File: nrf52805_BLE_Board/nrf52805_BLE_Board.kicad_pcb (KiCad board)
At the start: 2 copper layers, 27 parts, among them J1 TSW-103-23-H-S, J2 10118194-0001LF, J3 3220-10-0100-00, J4 TSW-107-23-H-S, J5 TSW-107-23-H-S, U1 BC805M, U2 CP2102N-Axx-xQFN28, U3 TCR3DF33_LMCT, Y1 CM9V-T1A-32.768KHZ-9PF-20PPM-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

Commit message: Finish layout
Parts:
- moved U2 193.4 mm to (58.0, 63.0), turned to 90 degrees
- moved J4 168.8 mm to (51.5, 45.5), turned to -90 degrees
- moved R5 150.0 mm to (57.9, 50.6)
- moved J5 149.6 mm to (71.4, 60.7), turned to 90 degrees
- moved L1 143.6 mm to (55.0, 74.4), turned to 90 degrees
- moved R3 143.2 mm to (70.5, 31.5)
- moved R4 142.6 mm to (70.5, 35.5)
- moved R2 142.3 mm to (59.8, 72.0)
- moved C7 140.3 mm to (64.5, 41.9), turned to 180 degrees
- moved L2 140.1 mm to (59.8, 70.0), turned to 180 degrees
- moved C8 138.7 mm to (70.5, 33.5), turned to 180 degrees
- moved R1 138.5 mm to (64.5, 60.1)
- moved C9 138.1 mm to (70.5, 37.5), turned to 180 degrees
- moved C6 136.0 mm to (59.8, 73.8)
- moved S1 134.8 mm to (52.3, 35.5), turned to 90 degrees
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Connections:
- C5 pad 1: unconnected-(C5-Pad1) -> Net-(C5-Pad1)
- R2 pad 2: unconnected-(R2-Pad2) -> Net-(R2-Pad2)
- U1 pad 2: /SWCLK -> /SWDCLK
- U3 pad 1: unconnected-(U3-Pad1) -> Net-(C6-Pad1)
- U3 pad 2: unconnected-(U3-Pad2) -> GND
- U3 pad 3: unconnected-(U3-Pad3) -> Net-(R2-Pad2)
- U3 pad 4: unconnected-(U3-Pad4) -> Net-(C5-Pad1)
- U3 pad 5: unconnected-(U3-Pad5) -> +3V3
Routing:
- net /P021: track 0.00 -> 51.5 mm
- net GND: track 0.00 -> 49.4 mm, vias 0 -> 53
- net +3V3: track 0.00 -> 49.1 mm, vias 0 -> 2
- net /P012: track 0.00 -> 43.9 mm
- net /P016: track 0.00 -> 39.1 mm, vias 0 -> 1
- net /SWDIO: track 0.00 -> 38.7 mm, vias 0 -> 5
- net /SWDCLK: track 0.00 -> 36.7 mm, vias 0 -> 3
- net /P020: track 0.00 -> 25.0 mm, vias 0 -> 2
- net /P005: track 0.00 -> 22.4 mm
- net /P018: track 0.00 -> 21.5 mm
- net /P014: track 0.00 -> 21.1 mm
- net /P004: track 0.00 -> 20.0 mm
- net /P000: track 0.00 -> 19.9 mm, vias 0 -> 1
- net /P001: track 0.00 -> 18.7 mm, vias 0 -> 1
- net Net-(U2-VBUS): track 0.00 -> 17.6 mm
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- added copper zone on B.Cu, net GND
- added copper zone on F.Cu, net GND
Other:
- board outline added: 22.9 x 50.8 mm

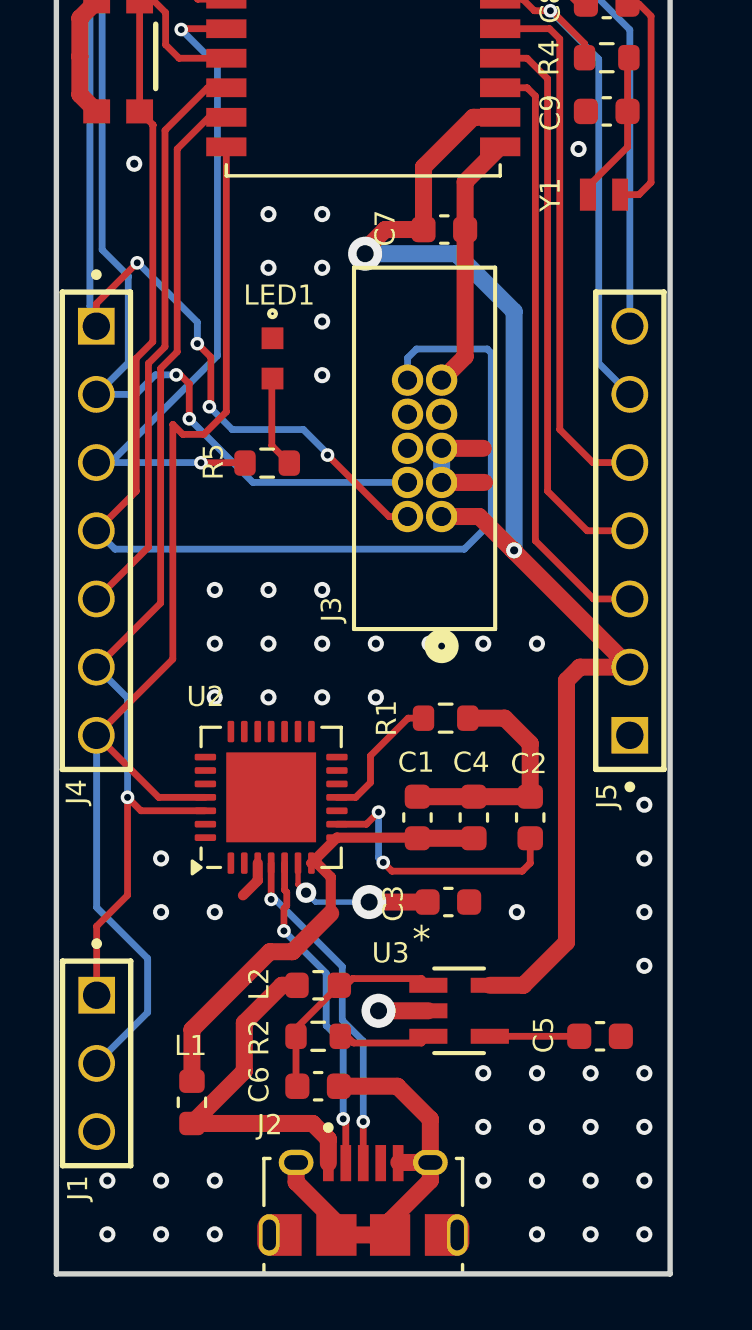
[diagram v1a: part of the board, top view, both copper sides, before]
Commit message: Add fiducials and silkscreen markings
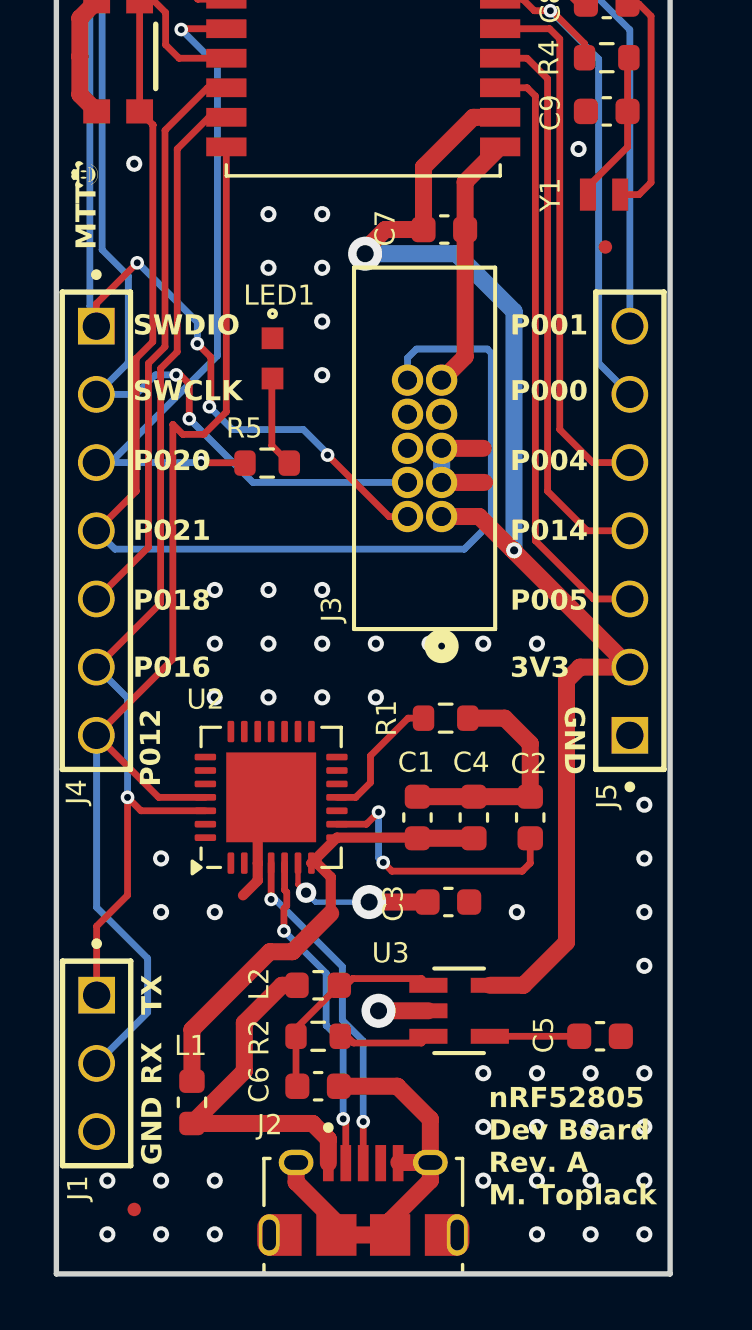
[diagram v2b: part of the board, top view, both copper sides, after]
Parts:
- added FD1: Fiducial, Fiducial:Fiducial_0.5mm_Mask1mm, F.Cu at (52.9, 78.4)
- added FD2: Fiducial, Fiducial:Fiducial_0.5mm_Mask1mm, F.Cu at (70.5, 42.5)
- added G***: LOGO, LOGO, F.Cu at (51.0, 39.9)
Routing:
- net GND: track 49.4 -> 52.0 mm
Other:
- board text added: "3V3"
- board text added: "GND"
- board text added: "MTT"
- board text added: "Matthew T. Toplack Design Fanstel BC805M Based nRF52805 Development Board"
- board text added: "P000"
- board text added: "P001"
- board text added: "P004"
- board text added: "P005"
- board text added: "P012"
- board text added: "P014"
- board text added: "P016"
- board text added: "P018"
- board text added: "P020"
- board text added: "P021"
- board text added: "RX"
- board text added: "SWCLK"
- board text added: "SWDIO"
- board text added: "TX"
- board text added: "nRF52805 Dev Board Rev. A M. Toplack"

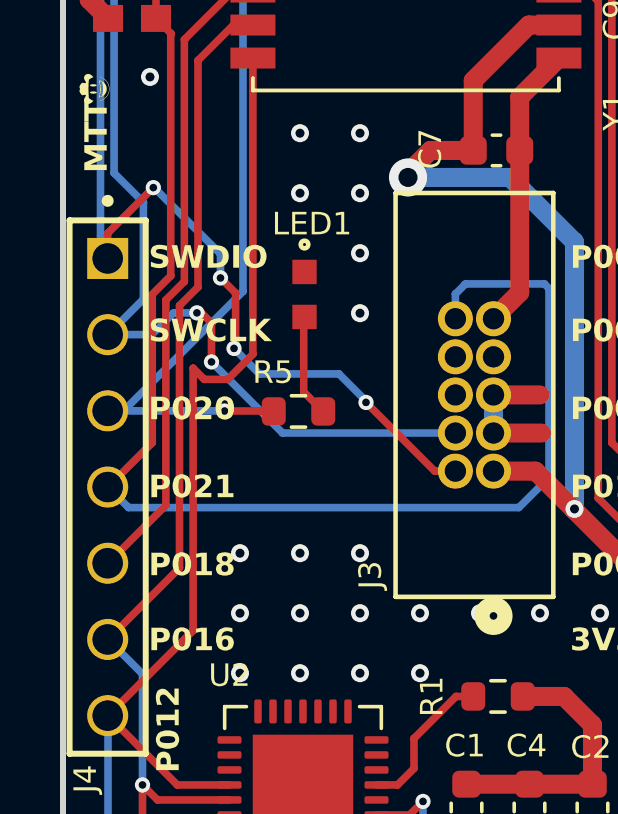
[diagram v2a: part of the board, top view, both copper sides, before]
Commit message: Correct issue with traces, add fiducials to schematic
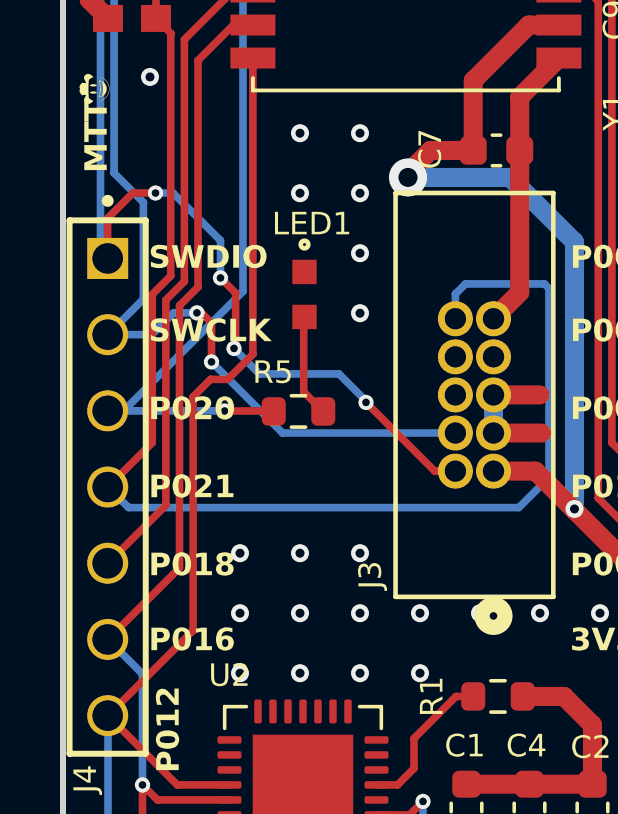
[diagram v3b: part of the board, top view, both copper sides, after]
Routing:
- net /P012: track 43.9 -> 43.1 mm
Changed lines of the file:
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@@
 			(outputformat 1)
 			(mirror no)
-			(drillshape 1)
+			(drillshape 0)
 			(scaleselection 1)
-			(outputdirectory "")
+			(outputdirectory "Gerbers/")
 		)
 	)
@@
 	(segment
 		(start 55.490659 49.531)
-		(end 54.709341 49.531)
+		(end 54.919 49.531)
 		(width 0.254)
 		(layer "F.Cu")
@@
 	)
 	(segment
-		(start 54.33717 49.158829)
-		(end 54.33717 57.90283)
+		(start 51.5 60.74)
+		(end 53.81 63.05)
 		(width 0.254)
 		(layer "F.Cu")
@@
 	)
 	(segment
-		(start 51.5 60.74)
-		(end 53.81 63.05)
+		(start 56.33 48.691659)
+		(end 55.490659 49.531)
 		(width 0.254)
 		(layer "F.Cu")
@@
 	)
 	(segment
-		(start 54.709341 49.531)
-		(end 54.33717 49.158829)
+		(start 53.81 63.05)
+		(end 55.55 63.05)
 		(width 0.254)
 		(layer "F.Cu")
@@
 	)
 	(segment
-		(start 56.33 38.82)
-		(end 56.33 48.691659)
+		(start 54.33717 50.11283)
+		(end 54.33717 57.90283)
 		(width 0.254)
 		(layer "F.Cu")
@@
 	)
 	(segment
-		(start 54.33717 57.90283)
-		(end 51.5 60.74)
+		(start 56.33 38.82)
+		(end 56.33 48.691659)
 		(width 0.254)
 		(layer "F.Cu")
@@
 	)
 	(segment
-		(start 53.81 63.05)
-		(end 55.55 63.05)
+		(start 54.33717 57.90283)
+		(end 51.5 60.74)
 		(width 0.254)
 		(layer "F.Cu")
@@
 	)
 	(segment
-		(start 56.33 48.691659)
-		(end 55.490659 49.531)
+		(start 54.919 49.531)
+		(end 54.33717 50.11283)
 		(width 0.254)
 		(layer "F.Cu")
@@
 	)
 	(segment
-		(start 53.011 43.139343)
-		(end 53.05 43.100343)
+		(start 51.489 44.161)
+		(end 51.489 45.5)
 		(width 0.254)
 		(layer "F.Cu")
@@
 	)
 	(segment
-		(start 51.489 44.661343)
-		(end 53.011 43.139343)
+		(start 52.330667 43.319333)
+		(end 51.489 44.161)
 		(width 0.254)
 		(layer "F.Cu")
@@
 	)
 	(segment
-		(start 51.489 45.5)
-		(end 51.489 44.661343)
+		(start 60.1 50.3)
+		(end 62.39 52.59)
 		(width 0.254)
 		(layer "F.Cu")
@@
 	)
 	(segment
-		(start 60.1 50.3)
-		(end 62.39 52.59)
+		(start 62.39 52.59)
+		(end 63.08 52.59)
 		(width 0.254)
 		(layer "F.Cu")
@@
 	)
 	(segment
-		(start 62.39 52.59)
-		(end 63.08 52.59)
+		(start 53.084001 43.319333)
+		(end 52.330667 43.319333)
 		(width 0.254)
 		(layer "F.Cu")
@@
 	)
 	(via
-		(at 53.011 43.139343)
+		(at 53.084001 43.319333)
 		(size 0.508)
 		(drill 0.254)
@@
 	)
 	(segment
-		(start 53.039343 43.139343)
-		(end 55.25 45.35)
+		(start 53.669333 43.319333)
+		(end 55.25 44.9)
 		(width 0.254)
 		(layer "B.Cu")
@@
 	)
 	(segment
-		(start 55.25 45.35)
-		(end 55.25 46.15)
-		(width 0.254)
-		(layer "B.Cu")
-		(net 40)
-	)
-	(segment
 		(start 52.404 30.85)
 		(end 51.75 31.504)
@@
 	)
 	(segment
-		(start 53.011 43.139343)
-		(end 53.039343 43.139343)
-		(width 0.254)
-		(layer "B.Cu")
-		(net 40)
-	)
-	(segment
 		(start 59.2 49.35)
 		(end 60.1 50.25)
@@
 	)
 	(segment
+		(start 53.084001 43.319333)
+		(end 53.669333 43.319333)
+		(width 0.254)
+		(layer "B.Cu")
+		(net 40)
+	)
+	(segment
 		(start 51.739 31.504)
 		(end 51.25 31.993)
 		(width 0.254)
 		(layer "B.Cu")
+		(net 40)
+	)
+	(segment
+		(start 55.25 44.9)
+		(end 55.25 46.15)
+		(width 0.254)
+		(layer "B.Cu")
